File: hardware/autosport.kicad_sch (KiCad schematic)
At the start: 10 parts, among them J2 AS022-55SN

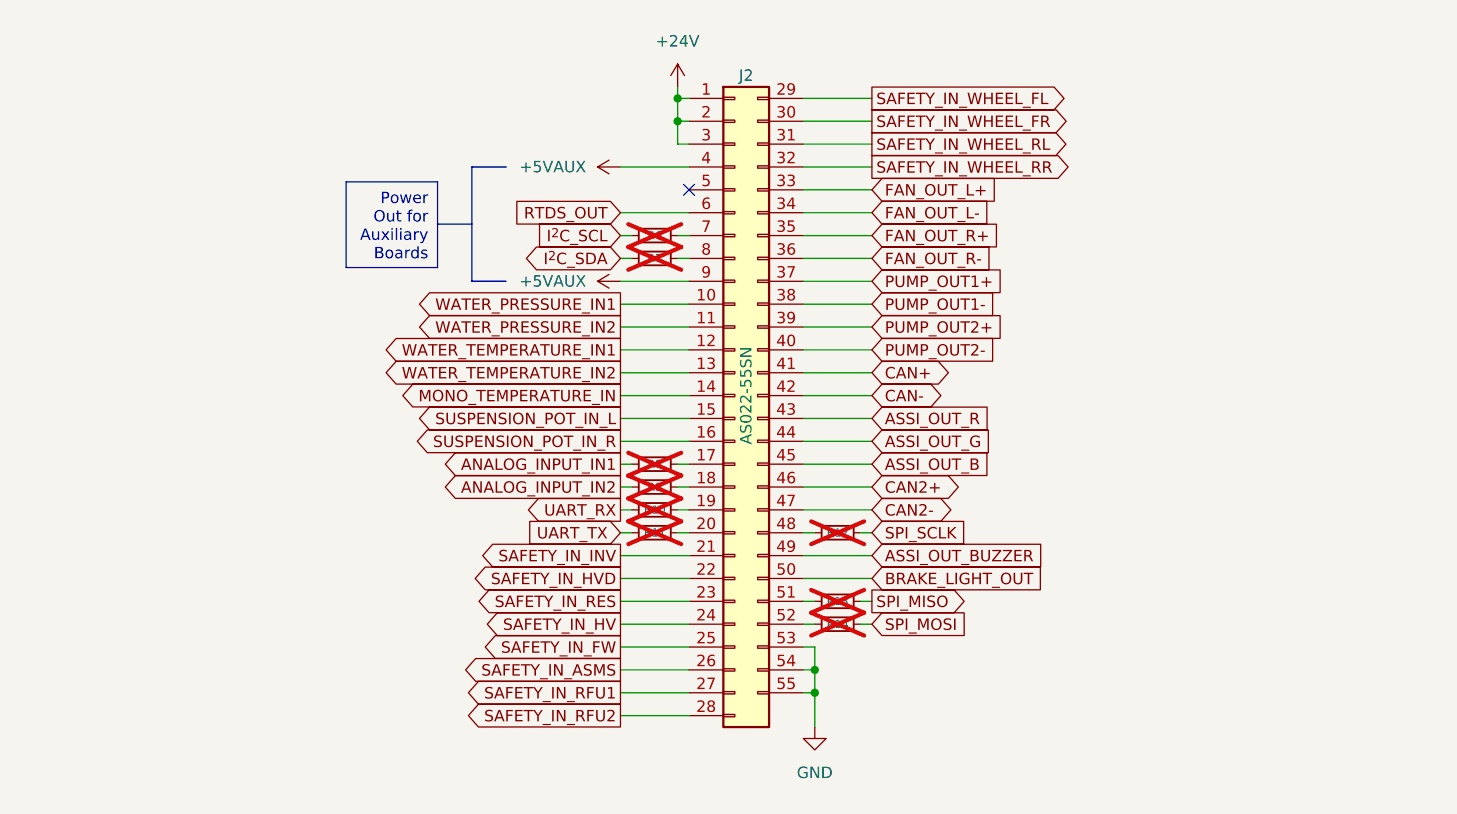
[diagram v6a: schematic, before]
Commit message: Improve the diagram based on the feedback
- add an input LC filter
- remove the USB connector
- add a programmer connector
- move optocouplers into a subsheet
- add a suspension tension meter IC
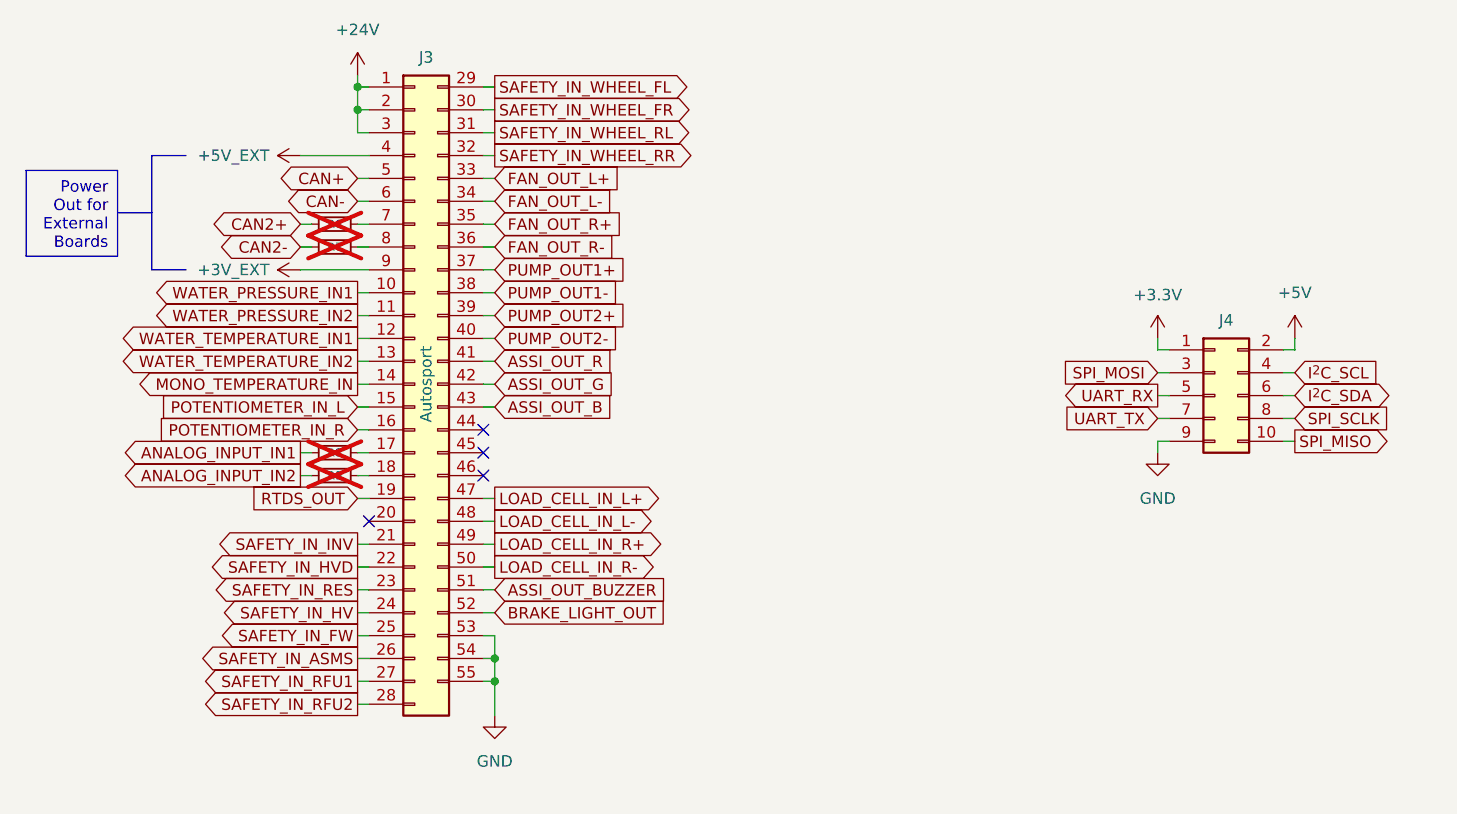
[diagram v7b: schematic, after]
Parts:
- removed R10, R11, R12, R13, R14: 0R, Resistor_SMD:R_0603_1608Metric, symbol Device:R_Small
- added J4: Auxiliary, Connector_PinHeader_2.54mm:PinHeader_2x05_P2.54mm_Vertical_SMD, symbol Connector_Generic:Conn_02x05_Odd_Even
- J3: renamed from J2; value AS022-55SN -> Autosport; Component (none) -> AS022-55SN
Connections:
- net ASSI_OUT_B: now also J3.43 (Pin_43); no longer J3.45 (Pin_45)
- net ASSI_OUT_BUZZER: now also J3.51 (Pin_51); no longer J3.49 (Pin_49)
- net ASSI_OUT_G: now also J3.42 (Pin_42); no longer J3.44 (Pin_44)
- net ASSI_OUT_R: now also J3.41 (Pin_41); no longer J3.43 (Pin_43)
- net BRAKE_LIGHT_OUT: now also J3.52 (Pin_52); no longer J3.50 (Pin_50)
- net CAN+: now also J3.5 (Pin_5); no longer J3.41 (Pin_41)
- net CAN-: now also J3.6 (Pin_6); no longer J3.42 (Pin_42)
- net CAN2+: now also R6.1; no longer J3.46 (Pin_46)
- net CAN2-: now also R7.1; no longer J3.47 (Pin_47)
- net GND: now also J4.9 (Pin_9)
- net I^{2}C_SCL: now also J4.4 (Pin_4); no longer R6.2
- net I^{2}C_SDA: now also J4.6 (Pin_6); no longer R7.2
- net RTDS_OUT: now also J3.19 (Pin_19); no longer J3.6 (Pin_6)
- net SPI_MISO: now also J4.10 (Pin_10)
- net SPI_MOSI: now also J4.3 (Pin_3)
- net SPI_SCLK: now also J4.8 (Pin_8)
- net UART_RX: now also J4.5 (Pin_5)
- net UART_TX: now also J4.7 (Pin_7)
- net at J3.8 (Pin_8): now also R7.2; no longer R7.1
- net LOAD_CELL_IN_L-: now reaches J3.48 (Pin_48)
- net at J3.7 (Pin_7): now also R6.2; no longer R6.1
- net +5VAUX renamed +3V_EXT
- net +3V_EXT: no longer J3.4 (Pin_4)
- net SUSPENSION_POT_IN_L renamed POTENTIOMETER_IN_L
- net SUSPENSION_POT_IN_R renamed POTENTIOMETER_IN_R
- new net +3.3V: J4.1 (Pin_1)
- new net +5V: J4.2 (Pin_2)
- new net +5V_EXT: J3.4 (Pin_4)
- new net LOAD_CELL_IN_L+: J3.47 (Pin_47)
- new net LOAD_CELL_IN_R+: J3.49 (Pin_49)
- new net LOAD_CELL_IN_R-: J3.50 (Pin_50)
- no-connect marks 1 -> 4
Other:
- title: (none) -> Autosport
- moved on the sheet: J3, R8, R9
